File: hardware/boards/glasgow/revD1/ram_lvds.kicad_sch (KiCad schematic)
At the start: 21 parts, among them J6 LVDS, U11 XccelaOPI, U12 XccelaOPI, U8 LFE5U-25F-8BG256x, Y3 Si5351A-B-GM

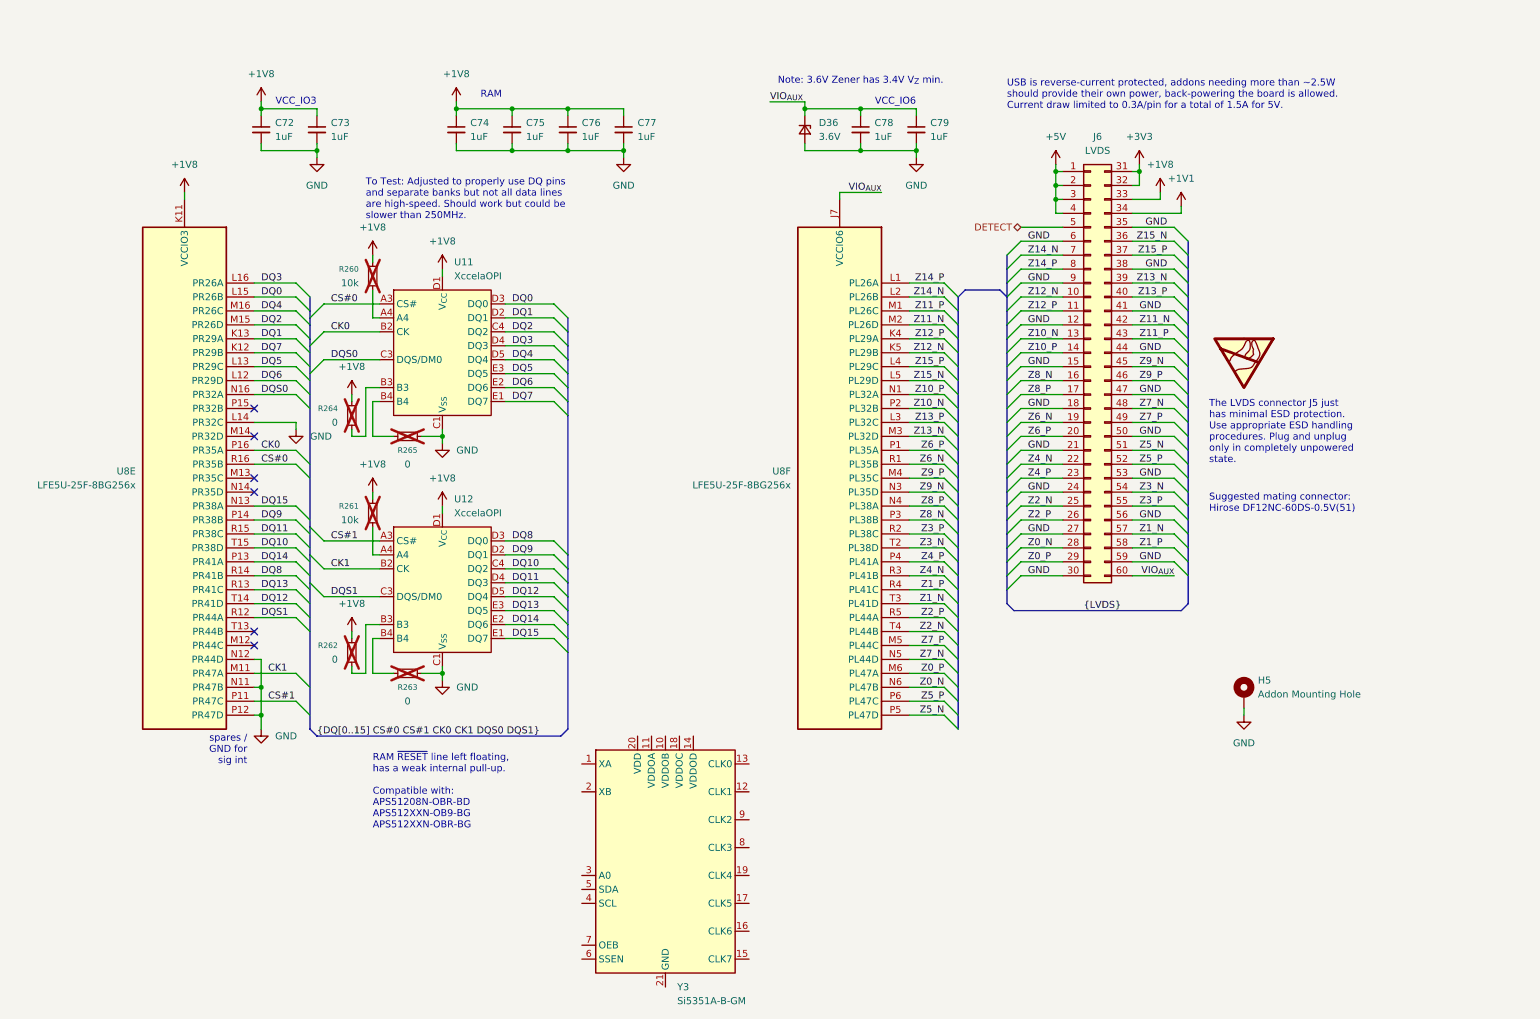
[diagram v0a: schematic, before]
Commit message: add clock gen
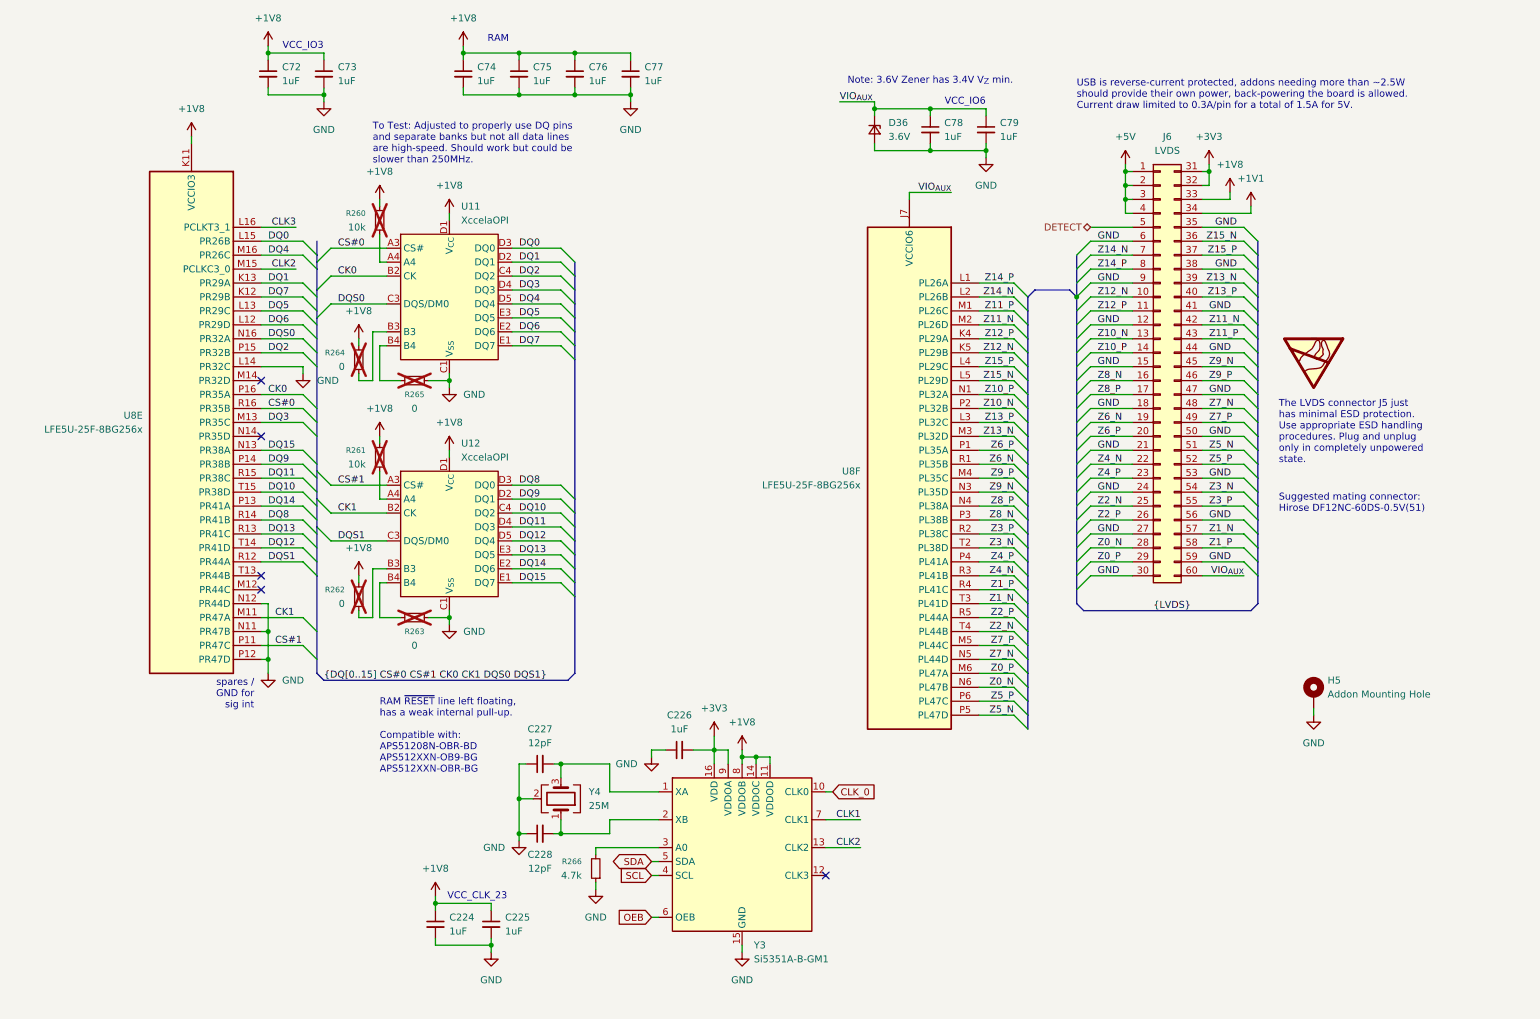
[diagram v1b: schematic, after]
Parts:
- removed Y3: Si5351A-B-GM, Package_DFN_QFN:QFN-20-1EP_4x4mm_P0.5mm_EP2.7x2.7mm, symbol Oscillator:Si5351A-B-GM
- added C224, C225, C226: 1uF, Capacitor_SMD:C_0201_0603Metric, symbol Device:C_Small
- added C227, C228: 12pF, Capacitor_SMD:C_0402_1005Metric, symbol Device:C_Small
- added R266: 4.7k, Resistor_SMD:R_0201_0603Metric, symbol Device:R_Small
- added Y3: Si5351A-B-GM1, Package_DFN_QFN:QFN-16-1EP_3x3mm_P0.5mm_EP1.75x1.75mm, symbol Means Of Circuit Design:Si5351A-B-GM1
- added Y4: 25M, Crystal:Crystal_SMD_3225-4Pin_3.2x2.5mm, symbol Device:Crystal_GND24
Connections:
- net +1V8: now also C224.1, C225.1, Y3.11 (VDDOD), Y3.14 (VDDOC), Y3.8 (VDDOB)
- net +3V3: now also C226.2, Y3.16 (VDD), Y3.9 (VDDOA)
- net DQ2: now also U8.P15 (PR32B); no longer U8.M15 (PR26D)
- net DQ3: now also U8.M13 (PR35C); no longer U8.L16 (PR26A)
- net GND: now also C224.2, C225.2, C226.1, C227.1, C228.1, R266.1, Y3.15 (GND), Y3.17 (GND), Y4.2 (G), Y4.4 (G)
- new net: C227.2, Y3.1 (XA), Y4.3
- new net: C228.2, Y3.2 (XB), Y4.1
- new net: R266.2, Y3.3 (A0)
- new net CLK1: Y3.7 (CLK1)
- new net CLK2: U8.M15 (PR26D), Y3.13 (CLK2)
- new net CLK3: U8.L16 (PR26A)
- new net CLK_0: Y3.10 (CLK0)
- new net OEB: Y3.6 (OEB)
- new net SCL: Y3.4 (SCL)
- new net SDA: Y3.5 (SDA)
- no-connect marks 6 -> 5
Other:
- note added: "VCC_CLK_23"
- moved on the sheet: C72, C73, C74, C75, C76, C77, C78, C79, D36, H5, J6, R260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

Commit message: start from 4 V, new inv bubo, more testpoints, synsyn through LS
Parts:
- added J11: CLK_EXT, Connector_Coaxial:U.FL_Molex_MCRF_73412-0110_Vertical, symbol Connector:Conn_Coaxial_Small
- added J12: FPGA_TP, symbol Connector_Generic:Conn_02x04_Top_Bottom
- added TP10: DQ0, symbol Connector:TestPoint_Small
- added TP11: DQ1, symbol Connector:TestPoint_Small
- added TP7: CS#0, symbol Connector:TestPoint_Small
- added TP8: CK0, symbol Connector:TestPoint_Small
- added TP9: DQS0, symbol Connector:TestPoint_Small
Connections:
- net CLK_0 is gone; now on net CLK0: Y3.10 (CLK0)
- net CK0: now also TP8.1
- net CLK1: now also U8.M15 (PR26D)
- net CLK2: now also J11.1 (In); no longer U8.M15 (PR26D)
- net CS#0: now also TP7.1
- net DQ0: now also TP10.1
- net DQ1: now also TP11.1
- net DQS0: now also TP9.1
- net GND: now also J11.2 (Ext), J12.5 (Pin_5), J12.6 (Pin_6), J12.7 (Pin_7), J12.8 (Pin_8); no longer U8.N11 (PR47B), U8.N12 (PR44D), U8.P12 (PR47D)
- net CLK_3: now reaches Y3.12 (CLK3)
- net T13: now reaches U8.T13 (PR44B)
- net T13: now also J12.1 (Pin_1)
- net CLK3 renamed CLK0
- new net N11: J12.4 (Pin_4), U8.N11 (PR47B)
- new net N12: J12.3 (Pin_3), U8.N12 (PR44D)
- new net P12: J12.2 (Pin_2), U8.P12 (PR47D)
- no-connect marks 5 -> 3
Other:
- note added: "TODO: GND test points near those."
- note removed: "spares / GND for sig int"

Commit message: wip
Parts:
- removed J12: FPGA_TP, symbol Connector_Generic:Conn_02x04_Top_Bottom
- added J12: FPGA_TP, Automated:Hirose_BM29_BM29B0.6-4DS_2-0.35V, symbol Connector_Generic_MountingPin:Conn_02x04_Top_Bottom_MountingPin
- added TP28: DQ1, Automated:TestPoint_Pad_D0.5mm, symbol Connector:TestPoint_Small
- TP10, TP11, TP7, TP8, TP9: footprint (none) -> Automated:TestPoint_Pad_D0.5mm
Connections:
- net +1V8: now also J12.1 (Pin_1), J12.5 (Pin_5)
- net GND: now also J12.4 (Pin_4), J12.8 (Pin_8), J12.MP (MountPin), TP28.1
- net N11: now also J12.2 (Pin_2)
- net N12: now also J12.7 (Pin_7)
- net P12: now also J12.3 (Pin_3)
- net T13: now also J12.6 (Pin_6)

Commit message: get routed
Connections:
- net DQ2: now also U8.M14 (PR32D); no longer U8.P15 (PR32B)
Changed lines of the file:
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@@
 	)
 	(no_connect
-		(at 59.69 119.38)
+		(at 59.69 76.2)
 	)
 	(no_connect
-		(at 59.69 81.28)
+		(at 59.69 119.38)
 	)
 	(no_connect
@@
 	)
 	(bus_entry
+		(at 69.85 76.2)
+		(size -2.54 -2.54)
+		(stroke
+			(width 0)
+			(type default)
+		)
+	)
+	(bus_entry
 		(at 69.85 64.77)
 		(size 2.54 -2.54)
@@
 	)
 	(bus_entry
-		(at 69.85 78.74)
+		(at 69.85 83.82)
 		(size -2.54 -2.54)
 		(stroke
@@
 	)
 	(bus_entry
-		(at 69.85 76.2)
-		(size -2.54 -2.54)
-		(stroke
-			(width 0)
-			(type default)
-		)
-	)
-	(bus_entry
 		(at 241.3 109.22)
 		(size -2.54 -2.54)
@@
 	(wire
 		(pts
-			(xy 59.69 78.74) (xy 67.31 78.74)
+			(xy 59.69 78.74) (xy 72.39 78.74)
 		)
 		(stroke
@@
 	(wire
 		(pts
-			(xy 59.69 76.2) (xy 67.31 76.2)
+			(xy 59.69 81.28) (xy 67.31 81.28)
 		)
 		(stroke
@@
 	(wire
 		(pts
-			(xy 67.31 80.01) (xy 67.31 78.74)
-		)
-		(stroke
-			(width 0)
-			(type default)
-		)
-	)
-	(wire
-		(pts
 			(xy 231.14 45.72) (xy 232.41 45.72)
 		)
@@
 	)
 	(label "DQ2"
-		(at 60.96 76.2 0)
+		(at 60.96 81.28 0)
 		(effects
 			(font
@@
 		)
 	)
-	(global_label "SDA"
-		(shape bidirectional)
-		(at 130.81 168.91 180)
-		(fields_autoplaced yes)
-		(effects
-			(font
-				(size 1.27 1.27)
-			)
-			(justify right)
-		)
-		(property "Intersheetrefs" "${INTERSHEET_REFS}"
-			(at 123.1454 168.91 0)
-			(hide yes)
-			(show_name no)
-			(do_not_autoplace no)
-			(effects
-				(font
-					(size 1.27 1.27)
-				)
-				(justify right)
-			)
-		)
-	)
-	(global_label "OEB"
+	(hierarchical_label "OEB"
 		(shape input)
 		(at 130.81 179.07 180)
-		(fields_autoplaced yes)
 		(effects
 			(font
@@
 			(justify right)
 		)
-		(property "Intersheetrefs" "${INTERSHEET_REFS}"
-			(at 124.0753 179.07 0)
-			(hide yes)
-			(show_name no)
-			(do_not_autoplace no)
-			(effects
-				(font
-					(size 1.27 1.27)
-				)
-				(justify right)
-			)
-		)
 	)
-	(global_label "SCL"
-		(shape input)
-		(at 130.81 171.45 180)
-		(fields_autoplaced yes)
+	(hierarchical_label "DETECT"
+		(shape bidirectional)
+		(at 210.82 53.34 180)
 		(effects
 			(font
@@
 			(justify right)
 		)
-		(property "Intersheetrefs" "${INTERSHEET_REFS}"
-			(at 124.3172 171.45 0)
-			(hide yes)
-			(show_name no)
-			(do_not_autoplace no)
-			(effects
-				(font
-					(size 1.27 1.27)
-				)
-				(justify right)
-			)
-		)
 	)
-	(global_label "CLK_3"
-		(shape input)
+	(hierarchical_label "CLK_3"
+		(shape output)
 		(at 163.83 171.45 0)
-		(fields_autoplaced yes)
 		(effects
 			(font
@@
 			(justify left)
 		)
-		(property "Intersheetrefs" "${INTERSHEET_REFS}"
-			(at 172.5604 171.45 0)
-			(hide yes)
-			(show_name no)
-			(do_not_autoplace no)
-			(effects
-				(font
-					(size 1.27 1.27)
-				)
-				(justify left)
+	)
+	(hierarchical_label "SDA"
+		(shape bidirectional)
+		(at 130.81 168.91 180)
+		(effects
+			(font
+				(size 1.27 1.27)
 			)
+			(justify right)
 		)
 	)
-	(hierarchical_label "DETECT"
-		(shape bidirectional)
-		(at 210.82 53.34 180)
+	(hierarchical_label "SCL"
+		(shape input)
+		(at 130.81 171.45 180)
 		(effects
 			(font
@@
 	(symbol
 		(lib_id "power:GND")
-		(at 67.31 80.01 0)
+		(at 72.39 78.74 0)
 		(unit 1)
 		(body_style 1)
@@
 		(fields_autoplaced yes)
 		(property "Reference" "#PWR0136"
-			(at 67.31 86.36 0)
+			(at 72.39 85.09 0)
 			(hide yes)
 			(show_name no)
@@
 		)
 		(property "Value" "GND"
-			(at 69.85 81.2799 0)
+			(at 74.93 80.0099 0)
 			(show_name no)
 			(do_not_autoplace no)
@@
 		)
 		(property "Footprint" ""
-			(at 67.31 80.01 0)
+			(at 72.39 78.74 0)
 			(hide yes)
 			(show_name no)
@@
 		)
 		(property "Datasheet" ""
-			(at 67.31 80.01 0)
+			(at 72.39 78.74 0)
 			(hide yes)
 			(show_name no)
@@
 		)
 		(property "Description" "Power symbol creates a global label with name \"GND\" , ground"
-			(at 67.31 80.01 0)
+			(at 72.39 78.74 0)
 			(hide yes)
 			(show_name no)

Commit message: wip pcb changes
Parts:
- H5: LCSC (none) -> C5457026; MPN (none) -> 9774050151R; now in the parts list
- J11: LCSC (none) -> C411563; MPN (none) -> KH-IPEX-K501-29; now fitted
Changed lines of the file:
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@@
 		(on_board yes)
 		(in_pos_files yes)
-		(dnp yes)
+		(dnp no)
 		(fields_autoplaced yes)
 		(property "Reference" "J11"
@@
 			)
 		)
+		(property "LCSC" "C411563"
+			(at 176.53 157.48 0)
+			(hide yes)
+			(show_name no)
+			(do_not_autoplace no)
+			(effects
+				(font
+					(size 1.27 1.27)
+				)
+			)
+		)
+		(property "MPN" "KH-IPEX-K501-29"
+			(at 176.53 157.48 0)
+			(hide yes)
+			(show_name no)
+			(do_not_autoplace no)
+			(effects
+				(font
+					(size 1.27 1.27)
+				)
+			)
+		)
 		(pin "2"
 		)
@@
 		(body_style 1)
 		(exclude_from_sim no)
-		(in_bom no)
+		(in_bom yes)
 		(on_board yes)
 		(in_pos_files yes)
@@
 			)
 		)
-		(property "KLC_S4.1" ""
+		(property "MPN" "9774050151R"
+			(at 251.46 138.43 0)
+			(hide yes)
+			(show_name no)
+			(do_not_autoplace no)
+			(effects
+				(font
+					(size 1.27 1.27)
+				)
+			)
+		)
+		(property "LCSC" "C5457026"
 			(at 251.46 138.43 0)
 			(hide yes)

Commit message: update bom
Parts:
- J12: LCSC (none) -> C3646565; MPN (none) -> BM29B0.6-4DS/2-0.35V(51)
- R260, R261: LCSC (none) -> C106225; MPN (none) -> RC0201FR-0710KL
- R262, R263, R264, R265: LCSC (none) -> C106227; MPN (none) -> RC0201FR-070RL
- TP10, TP11, TP7, TP8, TP9: now not fitted
- TP28: value DQ1 -> GND; now not fitted
- Y3: LCSC (none) -> C3609352; MPN (none) -> SI5351A-B-GM1
- Y4: LCSC (none) -> C9002; MPN (none) -> X322512MSB4SI
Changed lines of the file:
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@@
 			)
 		)
+		(property "LCSC" "C3646565"
+			(at 57.15 161.29 0)
+			(hide yes)
+			(show_name no)
+			(do_not_autoplace no)
+			(effects
+				(font
+					(size 1.27 1.27)
+				)
+			)
+		)
+		(property "MPN" "BM29B0.6-4DS/2-0.35V(51)"
+			(at 57.15 161.29 0)
+			(hide yes)
+			(show_name no)
+			(do_not_autoplace no)
+			(effects
+				(font
+					(size 1.27 1.27)
+				)
+			)
+		)
 		(pin "1"
 		)
@@
 			)
 		)
+		(property "LCSC" "C106227"
+			(at 87.63 124.46 90)
+			(hide yes)
+			(show_name no)
+			(do_not_autoplace no)
+			(effects
+				(font
+					(size 1.27 1.27)
+				)
+			)
+		)
+		(property "MPN" "RC0201FR-070RL"
+			(at 87.63 124.46 90)
+			(hide yes)
+			(show_name no)
+			(do_not_autoplace no)
+			(effects
+				(font
+					(size 1.27 1.27)
+				)
+			)
+		)
 		(pin "1"
 		)
@@
 			)
 		)
+		(property "LCSC" "C106227"
+			(at 87.63 81.28 90)
+			(hide yes)
+			(show_name no)
+			(do_not_autoplace no)
+			(effects
+				(font
+					(size 1.27 1.27)
+				)
+			)
+		)
+		(property "MPN" "RC0201FR-070RL"
+			(at 87.63 81.28 90)
+			(hide yes)
+			(show_name no)
+			(do_not_autoplace no)
+			(effects
+				(font
+					(size 1.27 1.27)
+				)
+			)
+		)
 		(pin "1"
 		)
@@
 		(on_board yes)
 		(in_pos_files yes)
-		(dnp no)
+		(dnp yes)
 		(fields_autoplaced yes)
 		(property "Reference" "TP10"
@@
 		(on_board yes)
 		(in_pos_files yes)
-		(dnp no)
+		(dnp yes)
 		(fields_autoplaced yes)
 		(property "Reference" "TP7"
@@
 			)
 		)
+		(property "LCSC" "C3609352"
+			(at 147.32 167.64 0)
+			(hide yes)
+			(show_name no)
+			(do_not_autoplace no)
+			(effects
+				(font
+					(size 1.27 1.27)
+				)
+			)
+		)
+		(property "MPN" "SI5351A-B-GM1"
+			(at 147.32 167.64 0)
+			(hide yes)
+			(show_name no)
+			(do_not_autoplace no)
+			(effects
+				(font
+					(size 1.27 1.27)
+				)
+			)
+		)
 		(pin "11"
 		)
@@
 			)
 		)
+		(property "LCSC" "C106225"
+			(at 81.28 52.07 0)
+			(hide yes)
+			(show_name no)
+			(do_not_autoplace no)
+			(effects
+				(font
+					(size 1.27 1.27)
+				)
+			)
+		)
+		(property "MPN" "RC0201FR-0710KL"
+			(at 81.28 52.07 0)
+			(hide yes)
+			(show_name no)
+			(do_not_autoplace no)
+			(effects
+				(font
+					(size 1.27 1.27)
+				)
+			)
+		)
 		(pin "1"
 		)
@@
 			)
 		)
-		(property "MPN" ""
+		(property "MPN" "X322512MSB4SI"
 			(at 39.37 203.2 0)
 			(hide yes)
@@
 			)
 		)
-		(property "LCSC" ""
+		(property "LCSC" "C9002"
 			(at 114.3 157.48 90)
 			(hide yes)
@@
 		(on_board yes)
 		(in_pos_files yes)
-		(dnp no)
+		(dnp yes)
 		(fields_autoplaced yes)
 		(property "Reference" "TP9"
@@
 			)
 		)
+		(property "LCSC" "C106227"
+			(at 77.47 120.65 0)
+			(hide yes)
+			(show_name no)
+			(do_not_autoplace no)
+			(effects
+				(font
+					(size 1.27 1.27)
+				)
+			)
+		)
+		(property "MPN" "RC0201FR-070RL"
+			(at 77.47 120.65 0)
+			(hide yes)
+			(show_name no)
+			(do_not_autoplace no)
+			(effects
+				(font
+					(size 1.27 1.27)
+				)
+			)
+		)
 		(pin "1"
 		)
@@
 			)
 		)
-		(property "KLC_S4.1" ""
-			(at 93.98 66.04 0)
-			(hide yes)
-			(show_name no)
-			(do_not_autoplace no)
-			(effects
-				(font
-					(size 1.27 1.27)
-				)
-			)
-		)
 		(pin "B3"
 		)
@@
 		(on_board yes)
 		(in_pos_files yes)
-		(dnp no)
+		(dnp yes)
 		(fields_autoplaced yes)
 		(property "Reference" "TP11"
@@
 		(on_board yes)
 		(in_pos_files yes)
-		(dnp no)
+		(dnp yes)
 		(fields_autoplaced yes)
 		(property "Reference" "TP8"
@@
 			)
 		)
+		(property "LCSC" "C106225"
+			(at 81.28 95.25 0)
+			(hide yes)
+			(show_name no)
+			(do_not_autoplace no)
+			(effects
+				(font
+					(size 1.27 1.27)
+				)
+			)
+		)
+		(property "MPN" "RC0201FR-0710KL"
+			(at 81.28 95.25 0)
+			(hide yes)
+			(show_name no)
+			(do_not_autoplace no)
+			(effects
+				(font
+					(size 1.27 1.27)
+				)
+			)
+		)
 		(pin "1"
 		)
@@
 			)
 		)
-		(property "KLC_S4.1" ""
-			(at 93.98 109.22 0)
-			(hide yes)
-			(show_name no)
-			(do_not_autoplace no)
-			(effects
-				(font
-					(size 1.27 1.27)
-				)
-			)
-		)
 		(pin "B3"
 		)
@@
 			)
 		)
+		(property "LCSC" "C106227"
+			(at 77.47 77.47 0)
+			(hide yes)
+			(show_name no)
+			(do_not_autoplace no)
+			(effects
+				(font
+					(size 1.27 1.27)
+				)
+			)
+		)
+		(property "MPN" "RC0201FR-070RL"
+			(at 77.47 77.47 0)
+			(hide yes)
+			(show_name no)
+			(do_not_autoplace no)
+			(effects
+				(font
+					(size 1.27 1.27)
+				)
+			)
+		)
 		(pin "1"
 		)
@@
 		(on_board yes)
 		(in_pos_files yes)
-		(dnp no)
+		(dnp yes)
 		(fields_autoplaced yes)
 		(property "Reference" "TP28"
@@
 			)
 		)
-		(property "Value" "DQ1"
+		(property "Value" "GND"
 			(at 133.35 85.0899 0)
 			(show_name no)
